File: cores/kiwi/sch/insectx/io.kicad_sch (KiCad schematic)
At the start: 15 parts, among them SW2 SW_DIP_x08, SW3 SW_DIP_x08, U3 74LS139, U43 TD62064, U51 X1-004, U56 X2-005, U57 X2-005, U58 X2-005, U59 X2-005, U60 X2-005

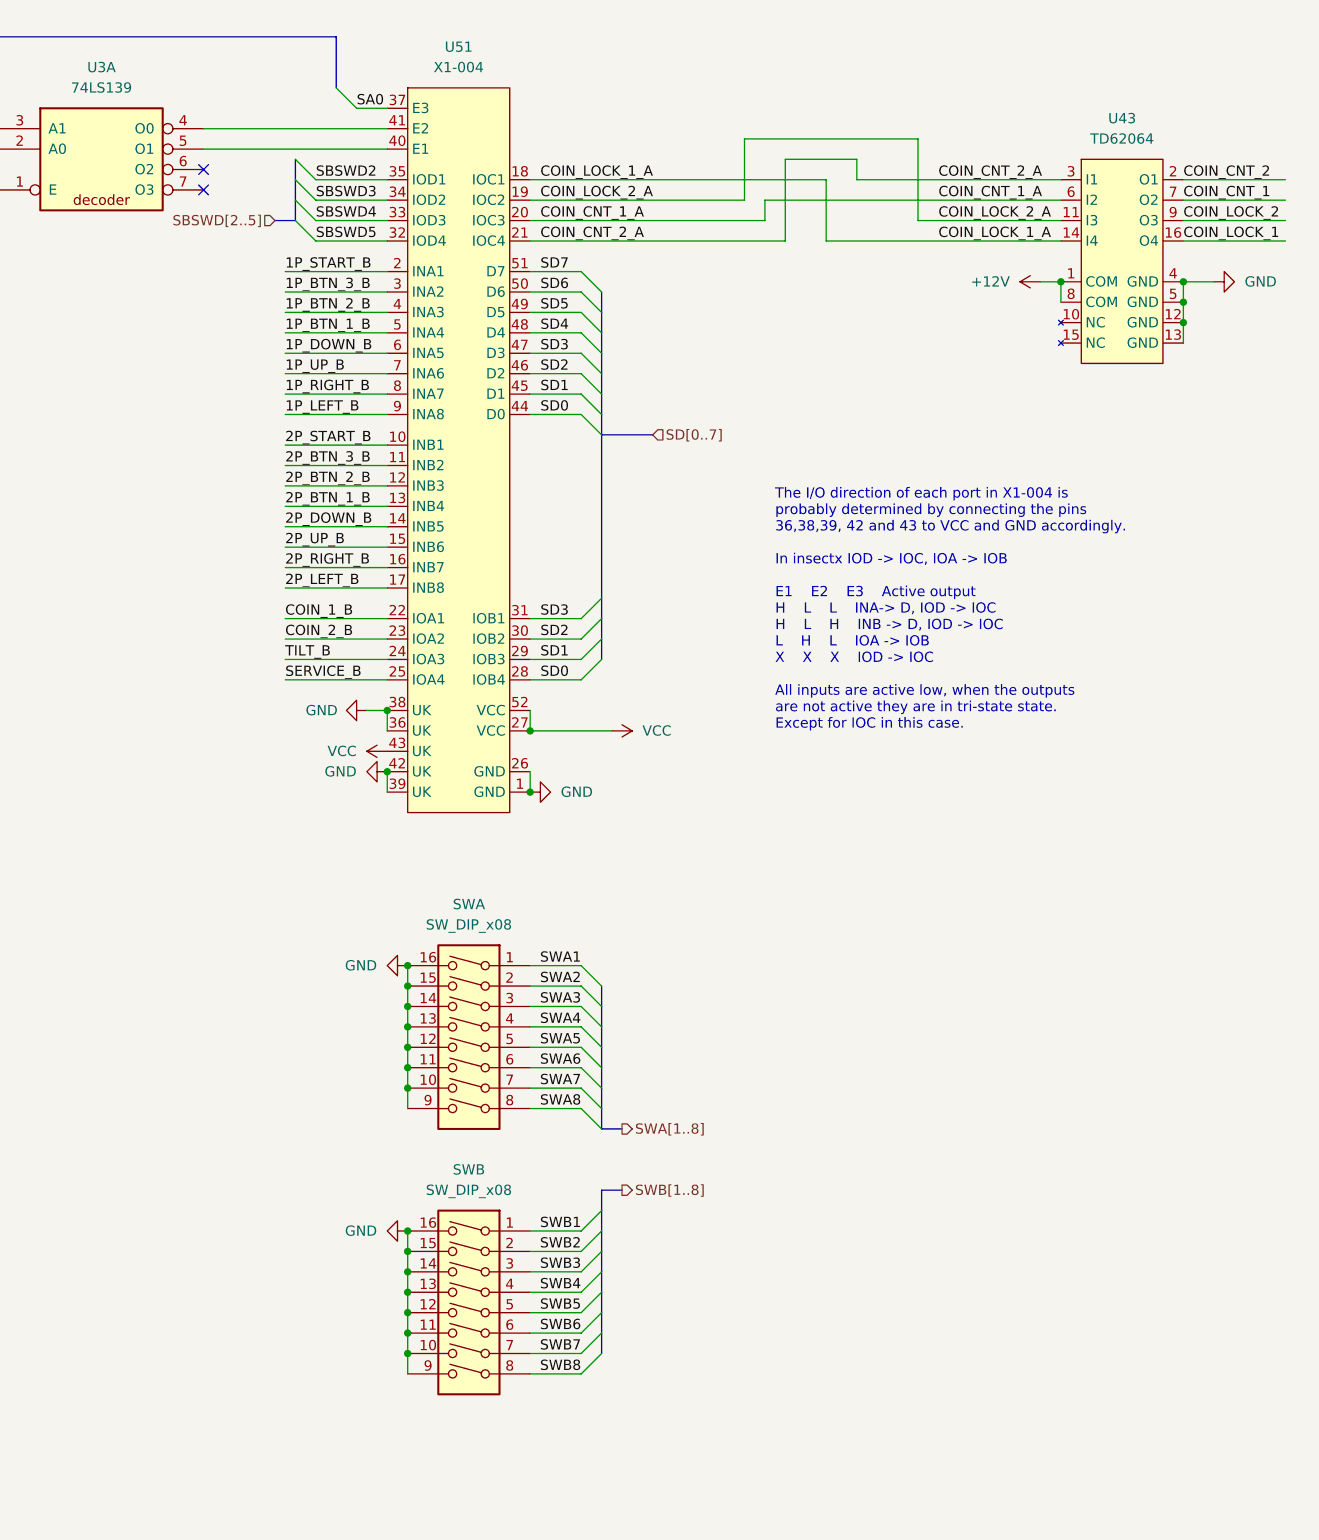
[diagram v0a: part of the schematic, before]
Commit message: Updated schematics according to: [insectx] schematic signals #22
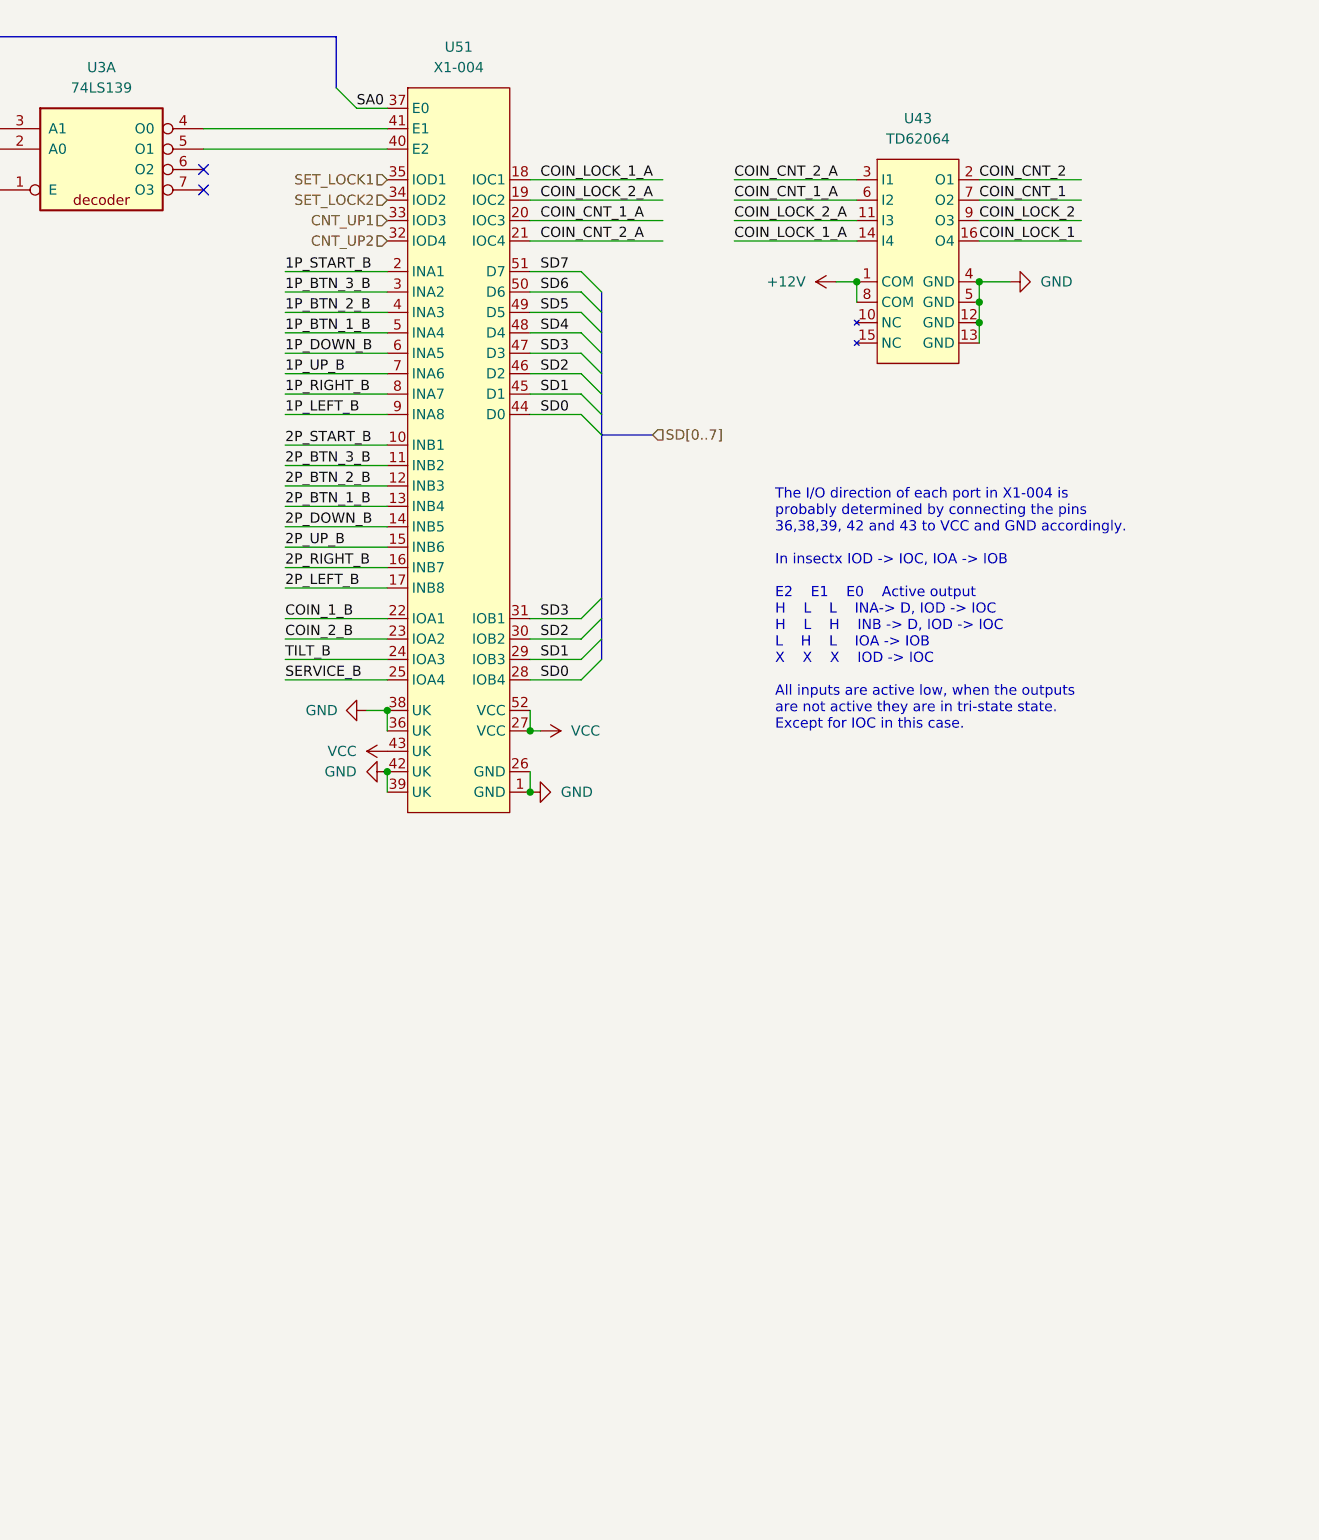
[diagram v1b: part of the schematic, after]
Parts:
- removed SW2, SW3: SW_DIP_x08, symbol Switch:SW_DIP_x08
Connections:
- net SBSWD2 renamed SET_LOCK1
- net SBSWD3 renamed SET_LOCK2
- net SBSWD4 renamed CNT_UP1
- net SBSWD5 renamed CNT_UP2
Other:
- note added: "The I/O direction of each port in X1-004 is probably determined by connecting the pins 36,38,39, 42 and 43 to VCC and GND accordingly. In insectx IOD -> IOC, IOA -> IOB E2 E1 E0 Active output H L L INA-> D, IOD -> IOC H L H INB -> D, IOD -> IOC L H L IOA -> IOB X X X IOD -> IOC All inputs are active low, when the outputs are not active they are in tri-state state. Except for IOC in this case."
- note removed: "The I/O direction of each port in X1-004 is probably determined by connecting the pins 36,38,39, 42 and 43 to VCC and GND accordingly. In insectx IOD -> IOC, IOA -> IOB E1 E2 E3 Active output H L L INA-> D, IOD -> IOC H L H INB -> D, IOD -> IOC L H L IOA -> IOB X X X IOD -> IOC All inputs are active low, when the outputs are not active they are in tri-state state. Except for IOC in this case."
- moved on the sheet: U43
